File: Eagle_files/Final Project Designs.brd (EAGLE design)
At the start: 5 parts

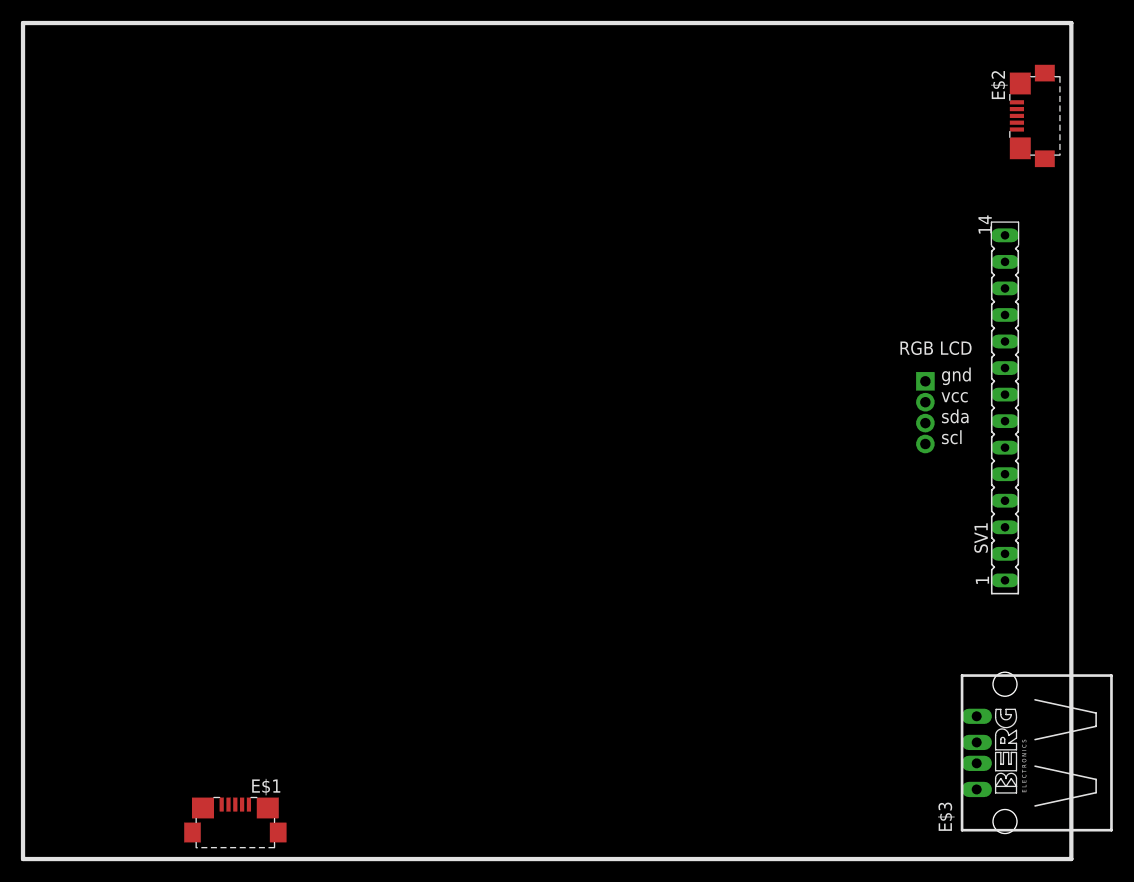
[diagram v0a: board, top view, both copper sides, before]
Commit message: Modified 14 pin header to include screw hole layout for lcd
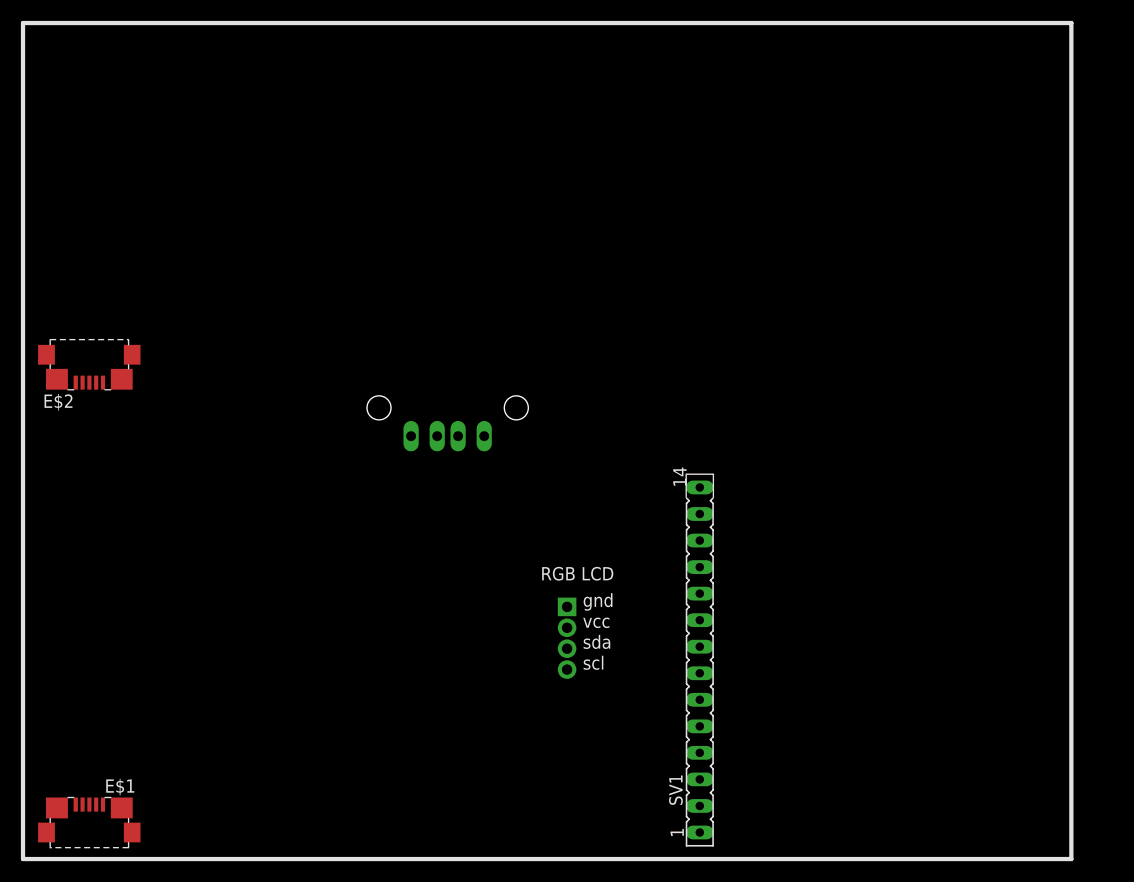
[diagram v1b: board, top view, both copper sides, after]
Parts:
- removed U$1: 4PIN_GROVE_CONNECTORUNIVERSAL_4_PIN_CONNECTOR, Tft_lcd_header:RGB_LCD
- added SV2: 4PIN_GROVE_CONNECTORUNIVERSAL_4_PIN_CONNECTOR, Tft_lcd_header:RGB_LCD
- moved E$2 94.3 mm to (6.35, 48.3), turned to 270 degrees
- moved E$3 62.7 mm to (40.6, 43.2), flipped to the bottom, turned to 180 degrees
- moved SV1 37.9 mm to (64.8, 20.3)
- moved E$1 14.0 mm to (6.35, 2.54)
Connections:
- net GND: now also SV2.P$1; no longer U$1.P$1
- net VCC: now also SV2.P$2; no longer U$1.P$2
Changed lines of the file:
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@@
 <layer number="37" name="tTest" color="7" fill="1" visible="no" active="yes"/>
 <layer number="38" name="bTest" color="7" fill="1" visible="no" active="yes"/>
-<layer number="39" name="tKeepout" color="4" fill="11" visible="yes" active="yes"/>
-<layer number="40" name="bKeepout" color="1" fill="11" visible="yes" active="yes"/>
-<layer number="41" name="tRestrict" color="4" fill="10" visible="yes" active="yes"/>
-<layer number="42" name="bRestrict" color="1" fill="10" visible="yes" active="yes"/>
-<layer number="43" name="vRestrict" color="2" fill="10" visible="yes" active="yes"/>
+<layer number="39" name="tKeepout" color="4" fill="11" visible="no" active="yes"/>
+<layer number="40" name="bKeepout" color="1" fill="11" visible="no" active="yes"/>
+<layer number="41" name="tRestrict" color="4" fill="10" visible="no" active="yes"/>
+<layer number="42" name="bRestrict" color="1" fill="10" visible="no" active="yes"/>
+<layer number="43" name="vRestrict" color="2" fill="10" visible="no" active="yes"/>
 <layer number="44" name="Drills" color="7" fill="1" visible="no" active="yes"/>
 <layer number="45" name="Holes" color="7" fill="1" visible="no" active="yes"/>
 <layer number="46" name="Milling" color="3" fill="1" visible="no" active="yes"/>
 <layer number="47" name="Measures" color="7" fill="1" visible="no" active="yes"/>
-<layer number="48" name="Document" color="7" fill="1" visible="yes" active="yes"/>
-<layer number="49" name="Reference" color="7" fill="1" visible="yes" active="yes"/>
-<layer number="50" name="dxf" color="7" fill="1" visible="yes" active="yes"/>
-<layer number="51" name="tDocu" color="7" fill="1" visible="yes" active="yes"/>
-<layer number="52" name="bDocu" color="7" fill="1" visible="yes" active="yes"/>
+<layer number="48" name="Document" color="7" fill="1" visible="no" active="yes"/>
+<layer number="49" name="Reference" color="7" fill="1" visible="no" active="yes"/>
+<layer number="50" name="dxf" color="7" fill="1" visible="no" active="yes"/>
+<layer number="51" name="tDocu" color="7" fill="1" visible="no" active="yes"/>
+<layer number="52" name="bDocu" color="7" fill="1" visible="no" active="yes"/>
 <layer number="53" name="tGND_GNDA" color="7" fill="9" visible="no" active="no"/>
 <layer number="54" name="bGND_GNDA" color="1" fill="9" visible="no" active="no"/>
-<layer number="56" name="wert" color="7" fill="1" visible="yes" active="yes"/>
+<layer number="56" name="wert" color="7" fill="1" visible="no" active="yes"/>
 <layer number="90" name="Modules" color="5" fill="1" visible="no" active="no"/>
 <layer number="91" name="Nets" color="2" fill="1" visible="no" active="no"/>
@@
 <layer number="98" name="Guide" color="6" fill="1" visible="no" active="no"/>
 <layer number="100" name="Muster" color="7" fill="1" visible="no" active="no"/>
-<layer number="101" name="Patch_Top" color="12" fill="4" visible="yes" active="yes"/>
-<layer number="102" name="Vscore" color="7" fill="1" visible="yes" active="yes"/>
-<layer number="104" name="Name" color="7" fill="1" visible="yes" active="yes"/>
-<layer number="116" name="Patch_BOT" color="9" fill="4" visible="yes" active="yes"/>
-<layer number="121" name="_tsilk" color="7" fill="1" visible="yes" active="yes"/>
-<layer number="122" name="_bsilk" color="7" fill="1" visible="yes" active="yes"/>
-<layer number="151" name="HeatSink" color="7" fill="1" visible="yes" active="yes"/>
-<layer number="200" name="200bmp" color="1" fill="10" visible="yes" active="yes"/>
-<layer number="201" name="201bmp" color="2" fill="10" visible="yes" active="yes"/>
-<layer number="202" name="202bmp" color="3" fill="10" visible="yes" active="yes"/>
-<layer number="203" name="203bmp" color="4" fill="10" visible="yes" active="yes"/>
-<layer number="204" name="204bmp" color="5" fill="10" visible="yes" active="yes"/>
-<layer number="205" name="205bmp" color="6" fill="10" visible="yes" active="yes"/>
-<layer number="206" name="206bmp" color="7" fill="10" visible="yes" active="yes"/>
-<layer number="207" name="207bmp" color="8" fill="10" visible="yes" active="yes"/>
-<layer number="208" name="208bmp" color="9" fill="10" visible="yes" active="yes"/>
+<layer number="101" name="Patch_Top" color="12" fill="4" visible="no" active="yes"/>
+<layer number="102" name="Vscore" color="7" fill="1" visible="no" active="yes"/>
+<layer number="104" name="Name" color="7" fill="1" visible="no" active="yes"/>
+<layer number="116" name="Patch_BOT" color="9" fill="4" visible="no" active="yes"/>
+<layer number="121" name="_tsilk" color="7" fill="1" visible="no" active="yes"/>
+<layer number="122" name="_bsilk" color="7" fill="1" visible="no" active="yes"/>
+<layer number="151" name="HeatSink" color="7" fill="1" visible="no" active="yes"/>
+<layer number="200" name="200bmp" color="1" fill="10" visible="no" active="yes"/>
+<layer number="201" name="201bmp" color="2" fill="10" visible="no" active="yes"/>
+<layer number="202" name="202bmp" color="3" fill="10" visible="no" active="yes"/>
+<layer number="203" name="203bmp" color="4" fill="10" visible="no" active="yes"/>
+<layer number="204" name="204bmp" color="5" fill="10" visible="no" active="yes"/>
+<layer number="205" name="205bmp" color="6" fill="10" visible="no" active="yes"/>
+<layer number="206" name="206bmp" color="7" fill="10" visible="no" active="yes"/>
+<layer number="207" name="207bmp" color="8" fill="10" visible="no" active="yes"/>
+<layer number="208" name="208bmp" color="9" fill="10" visible="no" active="yes"/>
 <layer number="250" name="Descript" color="3" fill="1" visible="no" active="no"/>
 <layer number="251" name="SMDround" color="12" fill="11" visible="no" active="no"/>
-<layer number="254" name="cooling" color="7" fill="1" visible="yes" active="yes"/>
+<layer number="254" name="cooling" color="7" fill="1" visible="no" active="yes"/>
 </layers>
 <board>
@@
 <wire x1="100.33" y1="80.01" x2="100.33" y2="0" width="0.4064" layer="25"/>
 <wire x1="100.33" y1="0" x2="0" y2="0" width="0.4064" layer="25"/>
+<wire x1="0" y1="49.53" x2="49.53" y2="49.53" width="0.4064" layer="104"/>
+<wire x1="49.53" y1="49.53" x2="49.53" y2="0" width="0.4064" layer="104"/>
 </plain>
 <attributes>
@@
 </autorouter>
 <elements>
-<element name="SV1" library="Tft_lcd_header" package="FE15" value="" x="93.98" y="44.45" rot="R90">
-<attribute name="OC_NEWARK" value="unknown" x="93.98" y="44.45" size="1.778" layer="27" rot="R90" display="off"/>
-<attribute name="MPN" value="" x="93.98" y="44.45" size="1.778" layer="27" rot="R90" display="off"/>
-<attribute name="OC_FARNELL" value="unknown" x="93.98" y="44.45" size="1.778" layer="27" rot="R90" display="off"/>
-<attribute name="MF" value="" x="93.98" y="44.45" size="1.778" layer="27" rot="R90" display="off"/>
+<element name="SV1" library="Tft_lcd_header" package="FE15" value="" x="64.77" y="20.32" rot="R90">
+<attribute name="OC_NEWARK" value="unknown" x="64.77" y="20.32" size="1.778" layer="27" rot="R90" display="off"/>
+<attribute name="MPN" value="" x="64.77" y="20.32" size="1.778" layer="27" rot="R90" display="off"/>
+<attribute name="OC_FARNELL" value="unknown" x="64.77" y="20.32" size="1.778" layer="27" rot="R90" display="off"/>
+<attribute name="MF" value="" x="64.77" y="20.32" size="1.778" layer="27" rot="R90" display="off"/>
 </element>
-<element name="U$1" library="Tft_lcd_header" package="RGB_LCD" value="4PIN_GROVE_CONNECTORUNIVERSAL_4_PIN_CONNECTOR" x="86.36" y="45.72"/>
-<element name="E$1" library="con-hirose" package="ZX62R-B-5P" value="" x="20.32" y="2.54" rot="R90"/>
-<element name="E$2" library="con-hirose" package="ZX62R-B-5P" value="" x="97.79" y="71.12" rot="R180"/>
-<element name="E$3" library="con-berg" package="PN87520" value="" x="93.98" y="10.16" rot="R90"/>
+<element name="SV2" library="Tft_lcd_header" package="RGB_LCD" value="4PIN_GROVE_CONNECTORUNIVERSAL_4_PIN_CONNECTOR" x="52.07" y="24.13"/>
+<element name="E$1" library="con-hirose" package="ZX62R-B-5P" value="" x="6.35" y="2.54" rot="R90"/>
+<element name="E$2" library="con-hirose" package="ZX62R-B-5P" value="" x="6.35" y="48.26" rot="R270"/>
+<element name="E$3" library="con-berg" package="PN87520" value="" x="40.64" y="43.18" rot="MR180"/>
 </elements>
 <signals>
 <signal name="GND">
-<contactref element="U$1" pad="P$1"/>
+<contactref element="SV2" pad="P$1"/>
 </signal>
 <signal name="VCC">
-<contactref element="U$1" pad="P$2"/>
+<contactref element="SV2" pad="P$2"/>
 </signal>
 </signals>
